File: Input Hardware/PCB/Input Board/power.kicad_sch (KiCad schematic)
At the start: 20 parts, among them U1 LM317_TO-252, U3 LM317_TO-252

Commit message: Revert "conflict resolution"
This reverts commit e2196486344c2f16c0f4e50e55e8bad7e306dbb3, reversing
changes made to 6978c7447e140ee759e19aaebffdac22097ec1b9.
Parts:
- C? (x2): footprint Capacitor_SMD:C_0603_1608Metric -> Capacitor_SMD:C_0402_1005Metric
- C? (x4): footprint Capacitor_SMD:C_0603_1608Metric -> (none)
- C? (x2): footprint Capacitor_SMD:C_0603_1608Metric -> Capacitor_SMD:C_0805_2012Metric
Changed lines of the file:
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@@
 			)
 		)
-		(property "Footprint" "Capacitor_SMD:C_0603_1608Metric"
+		(property "Footprint" "Capacitor_SMD:C_0402_1005Metric"
 			(at 159.0548 118.11 0)
 			(effects
@@
 			)
 		)
-		(property "Footprint" "Capacitor_SMD:C_0603_1608Metric"
+		(property "Footprint" "Capacitor_SMD:C_0402_1005Metric"
 			(at 157.7848 72.39 0)
 			(effects
@@
 			)
 		)
-		(property "Footprint" "Capacitor_SMD:C_0603_1608Metric"
+		(property "Footprint" ""
 			(at 116.5352 72.39 0)
 			(effects
@@
 			)
 		)
-		(property "Footprint" "Capacitor_SMD:C_0603_1608Metric"
+		(property "Footprint" "Capacitor_SMD:C_0805_2012Metric"
 			(at 166.6748 118.11 0)
 			(effects
@@
 			)
 		)
-		(property "Footprint" "Capacitor_SMD:C_0603_1608Metric"
+		(property "Footprint" ""
 			(at 72.0852 72.39 0)
 			(effects
@@
 			)
 		)
-		(property "Footprint" "Capacitor_SMD:C_0603_1608Metric"
+		(property "Footprint" ""
 			(at 72.0852 118.11 0)
 			(effects
@@
 			)
 		)
-		(property "Footprint" "Capacitor_SMD:C_0603_1608Metric"
+		(property "Footprint" "Capacitor_SMD:C_0805_2012Metric"
 			(at 165.4048 72.39 0)
 			(effects
@@
 			)
 		)
-		(property "Footprint" "Capacitor_SMD:C_0603_1608Metric"
+		(property "Footprint" ""
 			(at 116.5352 118.11 0)
 			(effects

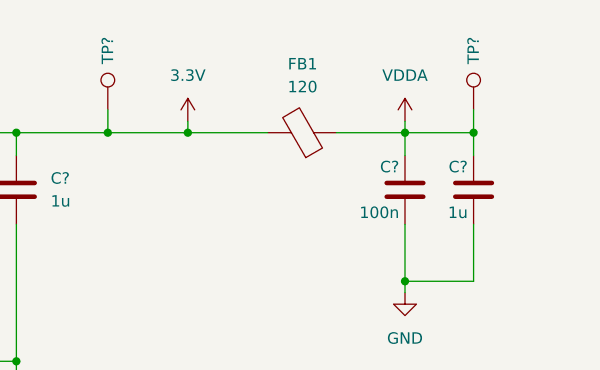
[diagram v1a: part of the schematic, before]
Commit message: Revert "images and pcb stuff"
This reverts commit 6978c7447e140ee759e19aaebffdac22097ec1b9.
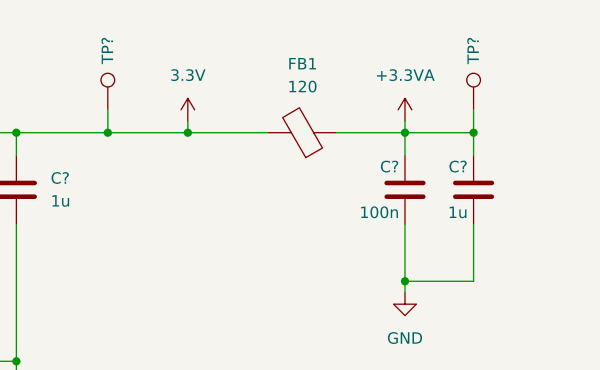
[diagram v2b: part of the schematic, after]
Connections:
- net VDDA renamed +3.3VA
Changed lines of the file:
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@@
 	)
 	(image
-		(at 359.41 86.36)
+		(at 364.49 88.9)
 		(data "iVBORw0KGgoAAAANSUhEUgAAArgAAAGkCAYAAADaPFZSAAAAAXNSR0IArs4c6QAAAARnQU1BAACx"
 			"jwv8YQUAAAAJcEhZcwAADsMAAA7DAcdvqGQAAKTbSURBVHhe7N0HfBNlHwfwX5Kmu3RAN3vvvaEF"
@@
 	)
 	(symbol
-		(lib_id "power:VDDA")
-		(at 158.75 60.96 0)
-		(mirror y)
-		(unit 1)
-		(exclude_from_sim no)
-		(in_bom yes)
-		(on_board yes)
-		(dnp no)
-		(fields_autoplaced yes)
-		(property "Reference" "#PWR0122"
-			(at 158.75 64.77 0)
-			(effects
-				(font
-					(size 1.27 1.27)
-				)
-				(hide yes)
-			)
-		)
-		(property "Value" "VDDA"
-			(at 158.75 55.88 0)
-			(effects
-				(font
-					(size 1.27 1.27)
-				)
-			)
-		)
-		(property "Footprint" ""
-			(at 158.75 60.96 0)
-			(effects
-				(font
-					(size 1.27 1.27)
-				)
-				(hide yes)
-			)
-		)
-		(property "Datasheet" ""
-			(at 158.75 60.96 0)
-			(effects
-				(font
-					(size 1.27 1.27)
-				)
-				(hide yes)
-			)
-		)
-		(property "Description" "Power symbol creates a global label with name \"VDDA\""
-			(at 158.75 60.96 0)
-			(effects
-				(font
-					(size 1.27 1.27)
-				)
-				(hide yes)
-			)
-		)
-		(pin "1"
-		)
-		(instances
-			(project "Input Board"
-				(path "/198ad8d1-66e3-4deb-889c-1af2b81e67c3/11f39170-493e-4ecf-a6ba-aee1374b2ff1"
-					(reference "#PWR0122")
-					(unit 1)
-				)
-			)
-		)
-	)
-	(symbol
 		(lib_name "GND_1")
 		(lib_id "power:GND")
@@
 	)
 	(symbol
+		(lib_id "power:+3.3VA")
+		(at 158.75 60.96 0)
+		(unit 1)
+		(exclude_from_sim no)
+		(in_bom yes)
+		(on_board yes)
+		(dnp no)
+		(fields_autoplaced yes)
+		(property "Reference" "#PWR0122"
+			(at 158.75 64.77 0)
+			(effects
+				(font
+					(size 1.27 1.27)
+				)
+				(hide yes)
+			)
+		)
+		(property "Value" "+3.3VA"
+			(at 158.75 55.88 0)
+			(effects
+				(font
+					(size 1.27 1.27)
+				)
+			)
+		)
+		(property "Footprint" ""
+			(at 158.75 60.96 0)
+			(effects
+				(font
+					(size 1.27 1.27)
+				)
+				(hide yes)
+			)
+		)
+		(property "Datasheet" ""
+			(at 158.75 60.96 0)
+			(effects
+				(font
+					(size 1.27 1.27)
+				)
+				(hide yes)
+			)
+		)
+		(property "Description" "Power symbol creates a global label with name \"+3.3VA\""
+			(at 158.75 60.96 0)
+			(effects
+				(font
+					(size 1.27 1.27)
+				)
+				(hide yes)
+			)
+		)
+		(pin "1"
+		)
+		(instances
+			(project "Input Board"
+				(path "/198ad8d1-66e3-4deb-889c-1af2b81e67c3/11f39170-493e-4ecf-a6ba-aee1374b2ff1"
+					(reference "#PWR0122")
+					(unit 1)
+				)
+			)
+		)
+	)
+	(symbol
 		(lib_id "Connector:TestPoint")
 		(at 125.73 59.69 0)
@@
 		(dnp no)
 		(fields_autoplaced yes)
-		(property "Reference" "#PWR093"
+		(property "Reference" "#PWR0167"
 			(at 134.62 64.77 0)
 			(effects
@@
 			(project ""
 				(path "/198ad8d1-66e3-4deb-889c-1af2b81e67c3/11f39170-493e-4ecf-a6ba-aee1374b2ff1"
-					(reference "#PWR093")
+					(reference "#PWR0167")
 					(unit 1)
 				)
@@
 		(dnp no)
 		(fields_autoplaced yes)
-		(property "Reference" "#PWR0132"
+		(property "Reference" "#PWR0141"
 			(at 158.75 86.36 0)
 			(effects
@@
 			(project "Input Board"
 				(path "/198ad8d1-66e3-4deb-889c-1af2b81e67c3/11f39170-493e-4ecf-a6ba-aee1374b2ff1"
-					(reference "#PWR0132")
+					(reference "#PWR0141")
 					(unit 1)
 				)

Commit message: More footprints
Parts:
- C? (x2): footprint Capacitor_SMD:C_0402_1005Metric -> Capacitor_SMD:C_0603_1608Metric
- C? (x4): footprint (none) -> Capacitor_SMD:C_0603_1608Metric
- C? (x2): footprint Capacitor_SMD:C_0805_2012Metric -> Capacitor_SMD:C_0603_1608Metric
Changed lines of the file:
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@@
 			)
 		)
-		(property "Footprint" "Capacitor_SMD:C_0402_1005Metric"
+		(property "Footprint" "Capacitor_SMD:C_0603_1608Metric"
 			(at 159.0548 118.11 0)
 			(effects
@@
 			)
 		)
-		(property "Footprint" "Capacitor_SMD:C_0402_1005Metric"
+		(property "Footprint" "Capacitor_SMD:C_0603_1608Metric"
 			(at 157.7848 72.39 0)
 			(effects
@@
 			)
 		)
-		(property "Footprint" ""
+		(property "Footprint" "Capacitor_SMD:C_0603_1608Metric"
 			(at 116.5352 72.39 0)
 			(effects
@@
 			)
 		)
-		(property "Footprint" "Capacitor_SMD:C_0805_2012Metric"
+		(property "Footprint" "Capacitor_SMD:C_0603_1608Metric"
 			(at 166.6748 118.11 0)
 			(effects
@@
 			)
 		)
-		(property "Footprint" ""
+		(property "Footprint" "Capacitor_SMD:C_0603_1608Metric"
 			(at 72.0852 72.39 0)
 			(effects
@@
 			)
 		)
-		(property "Footprint" ""
+		(property "Footprint" "Capacitor_SMD:C_0603_1608Metric"
 			(at 72.0852 118.11 0)
 			(effects
@@
 			)
 		)
-		(property "Footprint" "Capacitor_SMD:C_0805_2012Metric"
+		(property "Footprint" "Capacitor_SMD:C_0603_1608Metric"
 			(at 165.4048 72.39 0)
 			(effects
@@
 			)
 		)
-		(property "Footprint" ""
+		(property "Footprint" "Capacitor_SMD:C_0603_1608Metric"
 			(at 116.5352 118.11 0)
 			(effects
